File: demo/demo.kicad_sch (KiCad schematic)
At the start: 32 parts, among them SW1 SW_Push, SW10 SW_Push, SW11 SW_Push, SW12 SW_Push, SW13 SW_Push, SW14 SW_Push, SW15 SW_Push, SW16 SW_Push, SW2 SW_Push, SW3 SW_Push, SW4 SW_Push, SW5 SW_Push, SW6 SW_Push, SW7 SW_Push, SW8 SW_Push, SW9 SW_Push

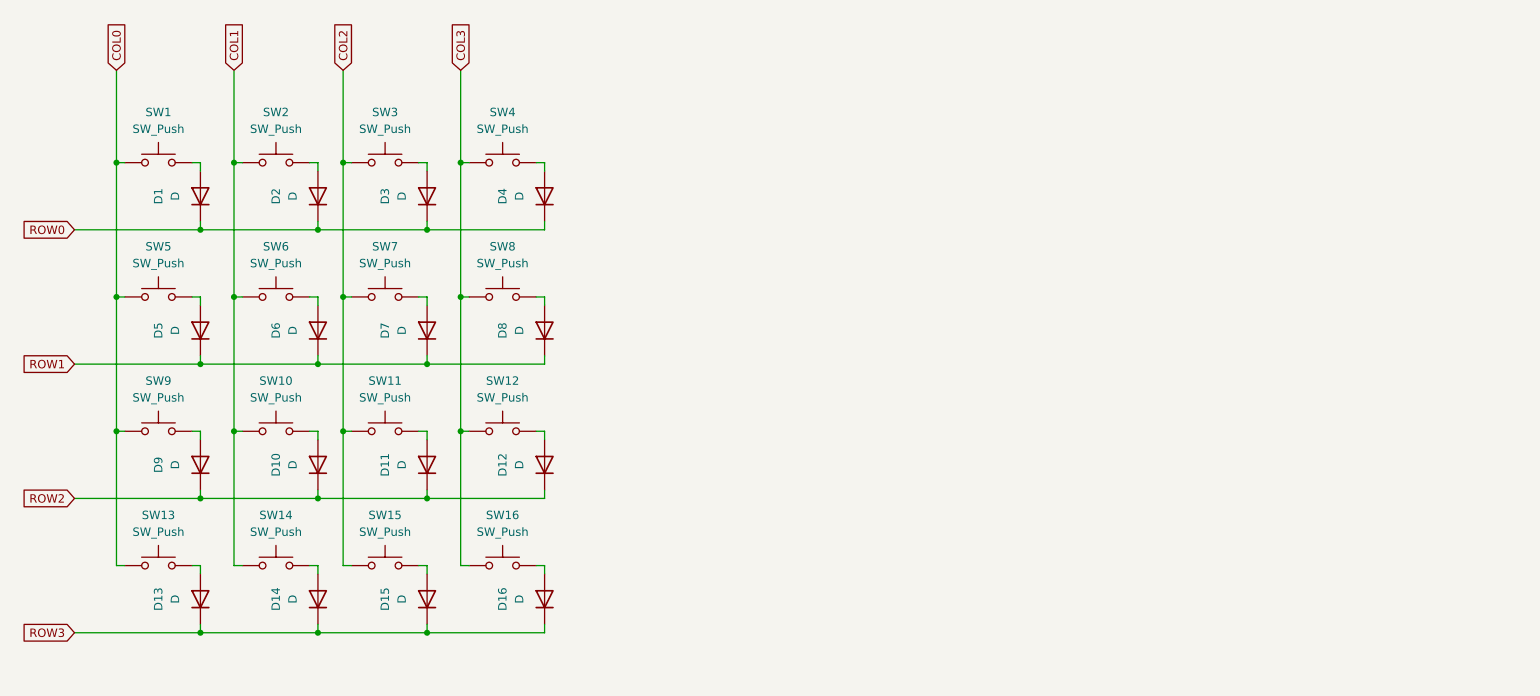
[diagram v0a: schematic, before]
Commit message: Add addressable RGB LEDs to demo board
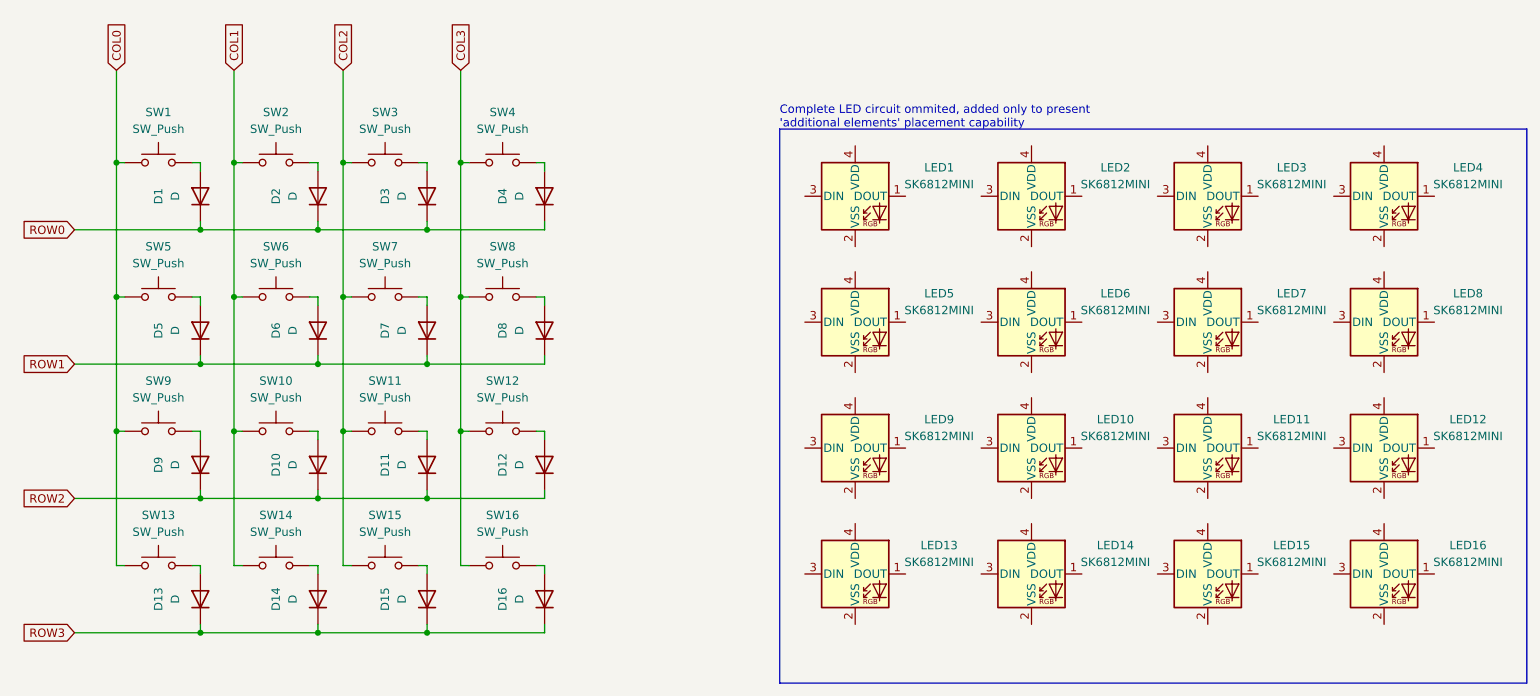
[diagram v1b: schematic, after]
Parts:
- added LED1, LED10, LED11, LED12, LED13, LED14, LED15, LED16, LED2, LED3, LED4, LED5, LED6, LED7, LED8, LED9: SK6812MINI, LED_SMD:LED_SK6812MINI_PLCC4_3.5x3.5mm_P1.75mm, symbol LED:SK6812MINI
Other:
- note added: "Complete LED circuit ommited, added only to present 'additional elements' placement capability"
